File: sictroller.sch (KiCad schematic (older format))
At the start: 21 parts

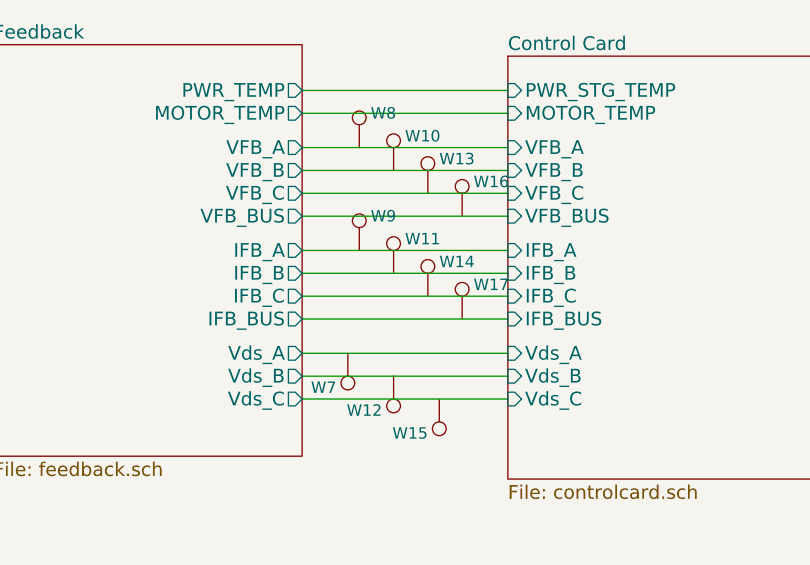
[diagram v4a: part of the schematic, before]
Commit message: Change J6 (microfit) pinning for better routing of HV
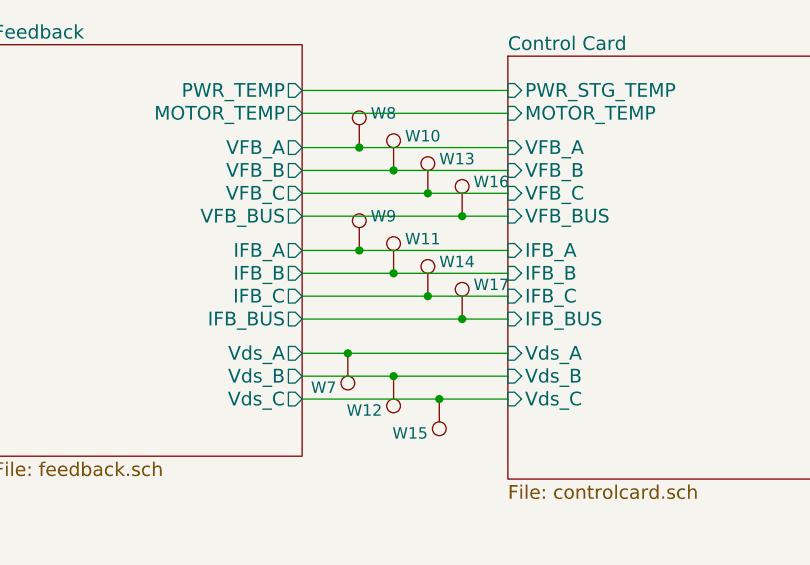
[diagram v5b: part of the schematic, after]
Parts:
- W10, W11, W12, W13, W14, W15, W16, W17, W20, W21, W22, W23: footprint (none) -> Measurement_Points:Measurement_Point_Round-SMD-Pad_Small
- W18, W19, W3, W4, W5, W6, W7, W8, W9: footprint (none) -> Measurement_Points:Measurement_Point_Round-TH_Small
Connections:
- net Control Card/IFB_A: now also W9.1
- net Control Card/IFB_B: now also W11.1
- net Control Card/IFB_BUS: now also W17.1
- net Control Card/IFB_C: now also W14.1
- net Control Card/VFB_A: now also W8.1
- net Control Card/VFB_B: now also W10.1
- net Control Card/VFB_BUS: now also W16.1
- net Control Card/VFB_C: now also W13.1
- net Control Card/Vds_A: now also W7.1
- net Control Card/Vds_B: now also W12.1
- net Control Card/Vds_C: now also W15.1
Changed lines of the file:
@@
 F 0 "W3" H 858 7670 50  0000 L CNN
 F 1 "TEST_1P" H 858 7579 50  0000 L CNN
-F 2 "" H 1000 7550 50  0000 C CNN
+F 2 "Measurement_Points:Measurement_Point_Round-TH_Small" H 1000 7550 50  0001 C CNN
 F 3 "" H 1000 7550 50  0000 C CNN
 	1    800  7550
@@
 F 0 "W4" H 1258 7670 50  0000 L CNN
 F 1 "TEST_1P" H 1258 7579 50  0000 L CNN
-F 2 "" H 1400 7550 50  0000 C CNN
+F 2 "Measurement_Points:Measurement_Point_Round-TH_Small" H 1400 7550 50  0001 C CNN
 F 3 "" H 1400 7550 50  0000 C CNN
 	1    1200 7550
@@
 $EndComp
 $Comp
-L GNDD #PWR1
+L GNDD #PWR01
 U 1 1 57A83FCA
 P 800 7550
-F 0 "#PWR1" H 800 7300 50  0001 C CNN
+F 0 "#PWR01" H 800 7300 50  0001 C CNN
 F 1 "GNDD" H 805 7377 50  0000 C CNN
 F 2 "" H 800 7550 50  0000 C CNN
@@
 $EndComp
 $Comp
-L GNDD #PWR2
+L GNDD #PWR02
 U 1 1 57A844D3
 P 1200 7550
-F 0 "#PWR2" H 1200 7300 50  0001 C CNN
+F 0 "#PWR02" H 1200 7300 50  0001 C CNN
 F 1 "GNDD" H 1205 7377 50  0000 C CNN
 F 2 "" H 1200 7550 50  0000 C CNN
@@
 F 0 "W5" H 1658 7670 50  0000 L CNN
 F 1 "TEST_1P" H 1658 7579 50  0000 L CNN
-F 2 "" H 1800 7550 50  0000 C CNN
+F 2 "Measurement_Points:Measurement_Point_Round-TH_Small" H 1800 7550 50  0001 C CNN
 F 3 "" H 1800 7550 50  0000 C CNN
 	1    1600 7550
@@
 F 0 "W6" H 2058 7670 50  0000 L CNN
 F 1 "TEST_1P" H 2058 7579 50  0000 L CNN
-F 2 "" H 2200 7550 50  0000 C CNN
+F 2 "Measurement_Points:Measurement_Point_Round-TH_Small" H 2200 7550 50  0001 C CNN
 F 3 "" H 2200 7550 50  0000 C CNN
 	1    2000 7550
@@
 $EndComp
 $Comp
-L GNDD #PWR3
+L GNDD #PWR03
 U 1 1 57A84AE2
 P 1600 7550
-F 0 "#PWR3" H 1600 7300 50  0001 C CNN
+F 0 "#PWR03" H 1600 7300 50  0001 C CNN
 F 1 "GNDD" H 1605 7377 50  0000 C CNN
 F 2 "" H 1600 7550 50  0000 C CNN
@@
 $EndComp
 $Comp
-L GNDD #PWR4
+L GNDD #PWR04
 U 1 1 57A84AE8
 P 2000 7550
-F 0 "#PWR4" H 2000 7300 50  0001 C CNN
+F 0 "#PWR04" H 2000 7300 50  0001 C CNN
 F 1 "GNDD" H 2005 7377 50  0000 C CNN
 F 2 "" H 2000 7550 50  0000 C CNN
@@
 F 0 "W18" H 7350 2450 50  0000 L CNN
 F 1 "TEST_1P" H 7358 2379 50  0001 L CNN
-F 2 "" H 7500 2350 50  0000 C CNN
+F 2 "Measurement_Points:Measurement_Point_Round-TH_Small" H 7500 2350 50  0001 C CNN
 F 3 "" H 7500 2350 50  0000 C CNN
 	1    7300 2350
@@
 F 0 "W20" H 7550 2600 50  0000 L CNN
 F 1 "TEST_1P" H 7558 2479 50  0001 L CNN
-F 2 "" H 7700 2450 50  0000 C CNN
+F 2 "Measurement_Points:Measurement_Point_Round-SMD-Pad_Small" H 7700 2450 50  0001 C CNN
 F 3 "" H 7700 2450 50  0000 C CNN
 	1    7500 2450
@@
 F 0 "W22" H 7750 2700 50  0000 L CNN
 F 1 "TEST_1P" H 7758 2579 50  0001 L CNN
-F 2 "" H 7900 2550 50  0000 C CNN
+F 2 "Measurement_Points:Measurement_Point_Round-SMD-Pad_Small" H 7900 2550 50  0001 C CNN
 F 3 "" H 7900 2550 50  0000 C CNN
 	1    7700 2550
@@
 F 0 "W19" H 7350 2800 50  0000 L CNN
 F 1 "TEST_1P" H 7358 2679 50  0001 L CNN
-F 2 "" H 7500 2650 50  0000 C CNN
+F 2 "Measurement_Points:Measurement_Point_Round-TH_Small" H 7500 2650 50  0001 C CNN
 F 3 "" H 7500 2650 50  0000 C CNN
 	1    7300 2650
@@
 F 0 "W21" H 7550 2900 50  0000 L CNN
 F 1 "TEST_1P" H 7558 2779 50  0001 L CNN
-F 2 "" H 7700 2750 50  0000 C CNN
+F 2 "Measurement_Points:Measurement_Point_Round-SMD-Pad_Small" H 7700 2750 50  0001 C CNN
 F 3 "" H 7700 2750 50  0000 C CNN
 	1    7500 2750
@@
 F 0 "W23" H 7750 3000 50  0000 L CNN
 F 1 "TEST_1P" H 7758 2879 50  0001 L CNN
-F 2 "" H 7900 2850 50  0000 C CNN
+F 2 "Measurement_Points:Measurement_Point_Round-SMD-Pad_Small" H 7900 2850 50  0001 C CNN
 F 3 "" H 7900 2850 50  0000 C CNN
 	1    7700 2850
@@
 F 0 "W7" H 4100 2950 50  0000 L CNN
 F 1 "TEST_1P" H 4108 2829 50  0001 L CNN
-F 2 "" H 4250 2800 50  0000 C CNN
+F 2 "Measurement_Points:Measurement_Point_Round-TH_Small" H 4250 2800 50  0001 C CNN
 F 3 "" H 4250 2800 50  0000 C CNN
 	1    4050 2800
@@
 F 0 "W12" H 4300 3050 50  0000 L CNN
 F 1 "TEST_1P" H 4308 2929 50  0001 L CNN
-F 2 "" H 4450 2900 50  0000 C CNN
+F 2 "Measurement_Points:Measurement_Point_Round-SMD-Pad_Small" H 4450 2900 50  0001 C CNN
 F 3 "" H 4450 2900 50  0000 C CNN
 	1    4250 2900
@@
 F 0 "W15" H 4500 3150 50  0000 L CNN
 F 1 "TEST_1P" H 4508 3029 50  0001 L CNN
-F 2 "" H 4650 3000 50  0000 C CNN
+F 2 "Measurement_Points:Measurement_Point_Round-SMD-Pad_Small" H 4650 3000 50  0001 C CNN
 F 3 "" H 4650 3000 50  0000 C CNN
 	1    4450 3000
@@
 F 0 "W8" H 4150 2050 50  0000 L CNN
 F 1 "TEST_1P" H 4158 1929 50  0001 L CNN
-F 2 "" H 4300 1900 50  0000 C CNN
+F 2 "Measurement_Points:Measurement_Point_Round-TH_Small" H 4300 1900 50  0001 C CNN
 F 3 "" H 4300 1900 50  0000 C CNN
 	1    4100 1900
@@
 F 0 "W10" H 4300 2150 50  0000 L CNN
 F 1 "TEST_1P" H 4308 2029 50  0001 L CNN
-F 2 "" H 4450 2000 50  0000 C CNN
+F 2 "Measurement_Points:Measurement_Point_Round-SMD-Pad_Small" H 4450 2000 50  0001 C CNN
 F 3 "" H 4450 2000 50  0000 C CNN
 	1    4250 2000
@@
 F 0 "W13" H 4450 2250 50  0000 L CNN
 F 1 "TEST_1P" H 4458 2129 50  0001 L CNN
-F 2 "" H 4600 2100 50  0000 C CNN
+F 2 "Measurement_Points:Measurement_Point_Round-SMD-Pad_Small" H 4600 2100 50  0001 C CNN
 F 3 "" H 4600 2100 50  0000 C CNN
 	1    4400 2100
@@
 F 0 "W16" H 4600 2350 50  0000 L CNN
 F 1 "TEST_1P" H 4608 2229 50  0001 L CNN
-F 2 "" H 4750 2200 50  0000 C CNN
+F 2 "Measurement_Points:Measurement_Point_Round-SMD-Pad_Small" H 4750 2200 50  0001 C CNN
 F 3 "" H 4750 2200 50  0000 C CNN
 	1    4550 2200
@@
 F 0 "W9" H 4150 2500 50  0000 L CNN
 F 1 "TEST_1P" H 4158 2379 50  0001 L CNN
-F 2 "" H 4300 2350 50  0000 C CNN
+F 2 "Measurement_Points:Measurement_Point_Round-TH_Small" H 4300 2350 50  0001 C CNN
 F 3 "" H 4300 2350 50  0000 C CNN
 	1    4100 2350
@@
 F 0 "W11" H 4300 2600 50  0000 L CNN
 F 1 "TEST_1P" H 4308 2479 50  0001 L CNN
-F 2 "" H 4450 2450 50  0000 C CNN
+F 2 "Measurement_Points:Measurement_Point_Round-SMD-Pad_Small" H 4450 2450 50  0001 C CNN
 F 3 "" H 4450 2450 50  0000 C CNN
 	1    4250 2450
@@
 F 0 "W14" H 4450 2700 50  0000 L CNN
 F 1 "TEST_1P" H 4458 2579 50  0001 L CNN
-F 2 "" H 4600 2550 50  0000 C CNN
+F 2 "Measurement_Points:Measurement_Point_Round-SMD-Pad_Small" H 4600 2550 50  0001 C CNN
 F 3 "" H 4600 2550 50  0000 C CNN
 	1    4400 2550
@@
 F 0 "W17" H 4600 2800 50  0000 L CNN
 F 1 "TEST_1P" H 4608 2679 50  0001 L CNN
-F 2 "" H 4750 2650 50  0000 C CNN
+F 2 "Measurement_Points:Measurement_Point_Round-SMD-Pad_Small" H 4750 2650 50  0001 C CNN
 F 3 "" H 4750 2650 50  0000 C CNN
 	1    4550 2650
 	1    0    0    -1
 $EndComp
+Connection ~ 4100 1900
+Connection ~ 4250 2000
+Connection ~ 4400 2100
+Connection ~ 4550 2200
+Connection ~ 4550 2650
+Connection ~ 4400 2550
+Connection ~ 4250 2450
+Connection ~ 4100 2350
+Connection ~ 4050 2800
+Connection ~ 4250 2900
+Connection ~ 4450 3000
 $EndSCHEMATC

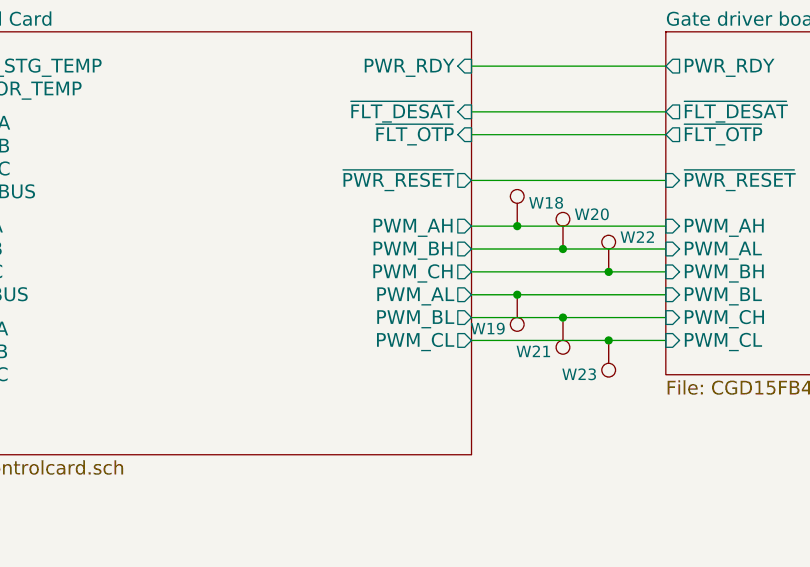
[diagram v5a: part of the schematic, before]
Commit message: Fix top-level PWM miswiring
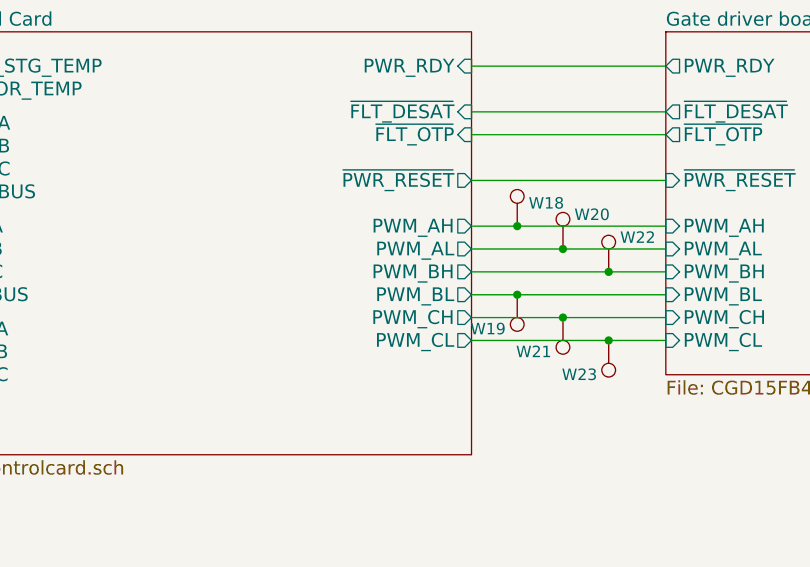
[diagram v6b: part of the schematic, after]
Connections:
- net Control Card/PWM_AL: now also W20.1; no longer W19.1
- net Control Card/PWM_BH: now also W22.1; no longer W20.1
- net Control Card/PWM_BL: now also W19.1; no longer W21.1
- net Control Card/PWM_CH: now also W21.1; no longer W22.1
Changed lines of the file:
@@
 F14 "Vds_C" I L 4750 3000 60
 F15 "PWM_AH" O R 7100 2350 60
-F16 "PWM_BH" O R 7100 2450 60
-F17 "PWM_CH" O R 7100 2550 60
-F18 "PWM_AL" O R 7100 2650 60
-F19 "PWM_BL" O R 7100 2750 60
+F16 "PWM_BH" O R 7100 2550 60
+F17 "PWM_CH" O R 7100 2750 60
+F18 "PWM_AL" O R 7100 2450 60
+F19 "PWM_BL" O R 7100 2650 60
 F20 "PWM_CL" O R 7100 2850 60
 F21 "~FLT_DESAT" I R 7100 1850 60

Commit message: PWM and faults routed
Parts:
- W19: footprint Measurement_Points:Measurement_Point_Round-TH_Small -> Measurement_Points:Measurement_Point_Round-SMD-Pad_Small
- W20: footprint Measurement_Points:Measurement_Point_Round-SMD-Pad_Small -> Measurement_Points:Measurement_Point_Round-TH_Small
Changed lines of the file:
@@
 F 0 "W20" H 7550 2600 50  0000 L CNN
 F 1 "TEST_1P" H 7558 2479 50  0001 L CNN
-F 2 "Measurement_Points:Measurement_Point_Round-SMD-Pad_Small" H 7700 2450 50  0001 C CNN
+F 2 "Measurement_Points:Measurement_Point_Round-TH_Small" H 7700 2450 50  0001 C CNN
 F 3 "" H 7700 2450 50  0000 C CNN
 	1    7500 2450
@@
 F 0 "W19" H 7350 2800 50  0000 L CNN
 F 1 "TEST_1P" H 7358 2679 50  0001 L CNN
-F 2 "Measurement_Points:Measurement_Point_Round-TH_Small" H 7500 2650 50  0001 C CNN
+F 2 "Measurement_Points:Measurement_Point_Round-SMD-Pad_Small" H 7500 2650 50  0001 C CNN
 F 3 "" H 7500 2650 50  0000 C CNN
 	1    7300 2650

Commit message: Layout complete
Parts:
- removed W11, W14, W17: TEST_1P, Measurement_Points:Measurement_Point_Round-SMD-Pad_Small, symbol TEST_1P
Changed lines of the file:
@@
-	1    0    0    -1
-$EndComp
-$Comp
-L TEST_1P W11
-U 1 1 57A8F295
-P 4250 2450
-F 0 "W11" H 4300 2600 50  0000 L CNN
-F 1 "TEST_1P" H 4308 2479 50  0001 L CNN
-F 2 "Measurement_Points:Measurement_Point_Round-SMD-Pad_Small" H 4450 2450 50  0001 C CNN
-F 3 "" H 4450 2450 50  0000 C CNN
-	1    4250 2450
-	1    0    0    -1
-$EndComp
-$Comp
-L TEST_1P W14
-U 1 1 57A8F404
-P 4400 2550
-F 0 "W14" H 4450 2700 50  0000 L CNN
-F 1 "TEST_1P" H 4458 2579 50  0001 L CNN
-F 2 "Measurement_Points:Measurement_Point_Round-SMD-Pad_Small" H 4600 2550 50  0001 C CNN
-F 3 "" H 4600 2550 50  0000 C CNN
-	1    4400 2550
-	1    0    0    -1
-$EndComp
-$Comp
-L TEST_1P W17
-U 1 1 57A8F574
-P 4550 2650
-F 0 "W17" H 4600 2800 50  0000 L CNN
-F 1 "TEST_1P" H 4608 2679 50  0001 L CNN
-F 2 "Measurement_Points:Measurement_Point_Round-SMD-Pad_Small" H 4750 2650 50  0001 C CNN
-F 3 "" H 4750 2650 50  0000 C CNN
-	1    4550 2650
 	1    0    0    -1
 $EndComp
@@
 Connection ~ 4400 2100
 Connection ~ 4550 2200
-Connection ~ 4550 2650
-Connection ~ 4400 2550
-Connection ~ 4250 2450
 Connection ~ 4100 2350
 Connection ~ 4050 2800
